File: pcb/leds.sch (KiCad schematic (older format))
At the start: 163 parts, among them K000 1.5U, K001 1U, K002 1U, K003 1U, K004 1U, K005 1U, K006 1U, K007 1U, K008 1U, K009 1U, K010 1U, K011 1U, K012 1U, K013 1.5U, K100 1.5U, K101 1U, K102 1U, K103 1U, K104 1U, K105 1U, K106 1U, K107 1U, K108 1U, K109 1U, K110 1U, K111 1U, K112 1U, K113 1.5U, K200 1.5U, K201 1U, K202 1U, K203 1U, K204 1U, K205 1U, K206 1U, K207 1U, K208 1U, K209 1U, K210 1U, K211 1U, K212 1U, K213 1.5U, K300 1.5U, K301 1U, K302 1U, K303 1U, K304 1U, K305 1U, K306 1U, K307 1U, K308 1U, K309 1U, K310 1U, K311 1U, K312 1U, K313 1.5U, K400 1.5U, K401 1U, K402 1U, K403 1U, K404 1U, K405 1U, K406 1U, K407 1U, K408 1U, K409 1U, K410 1U, K411 1U, K412 1U, K413 1.5U

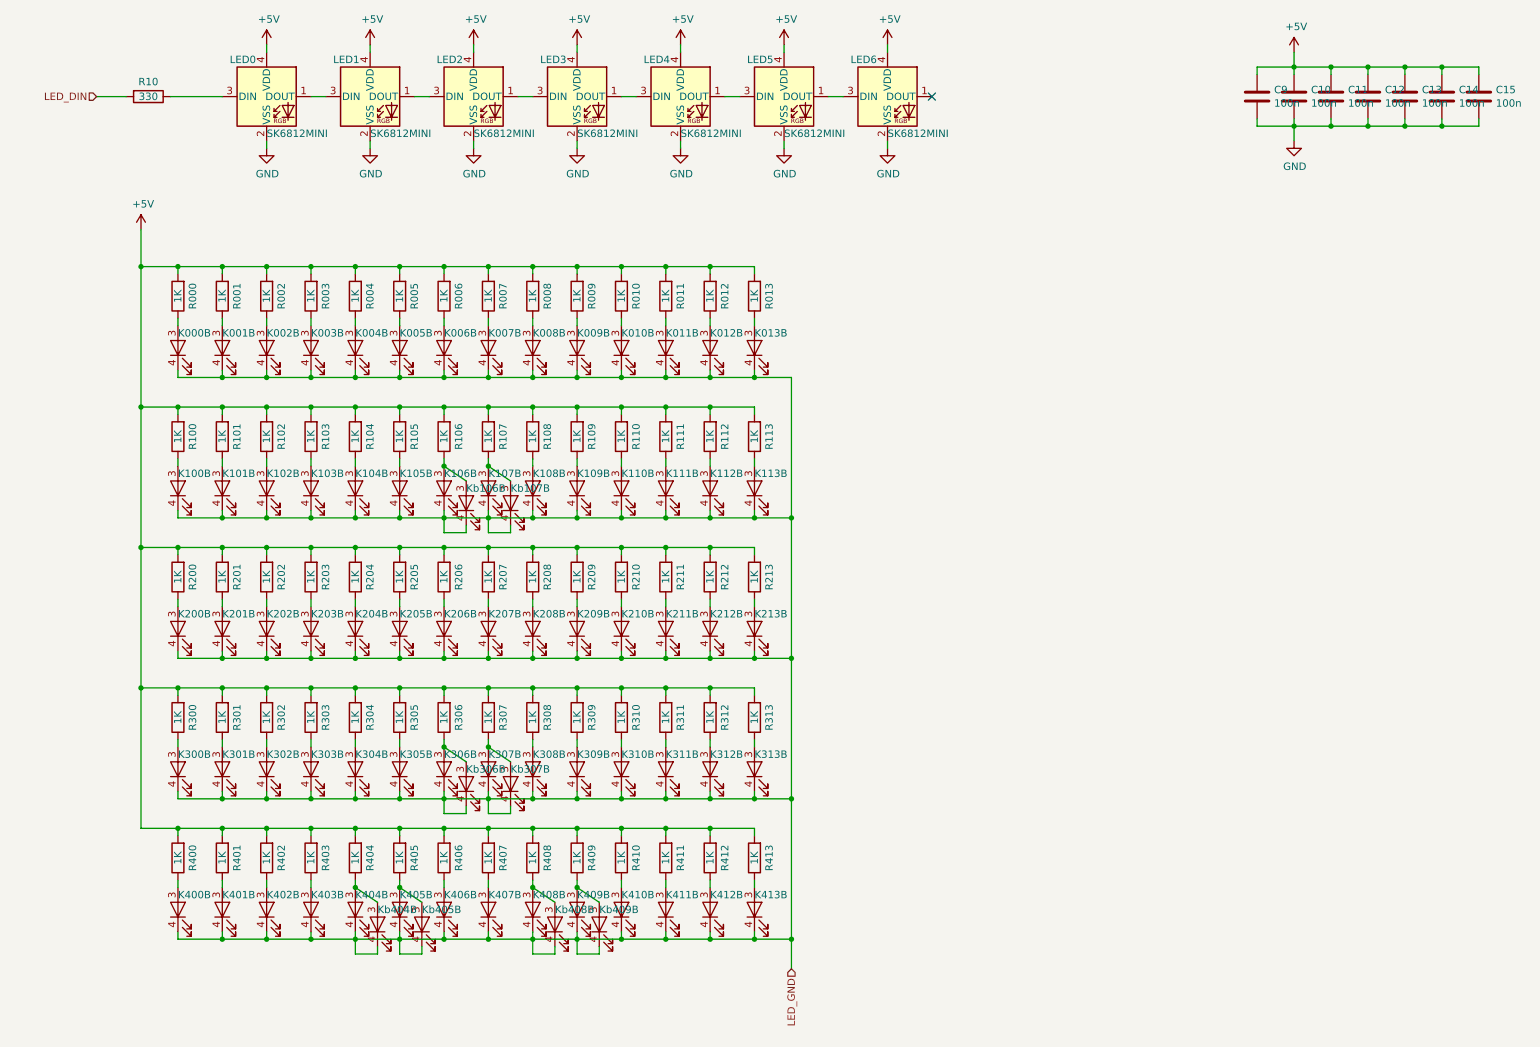
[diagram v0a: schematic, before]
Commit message: IS31 Led matrix
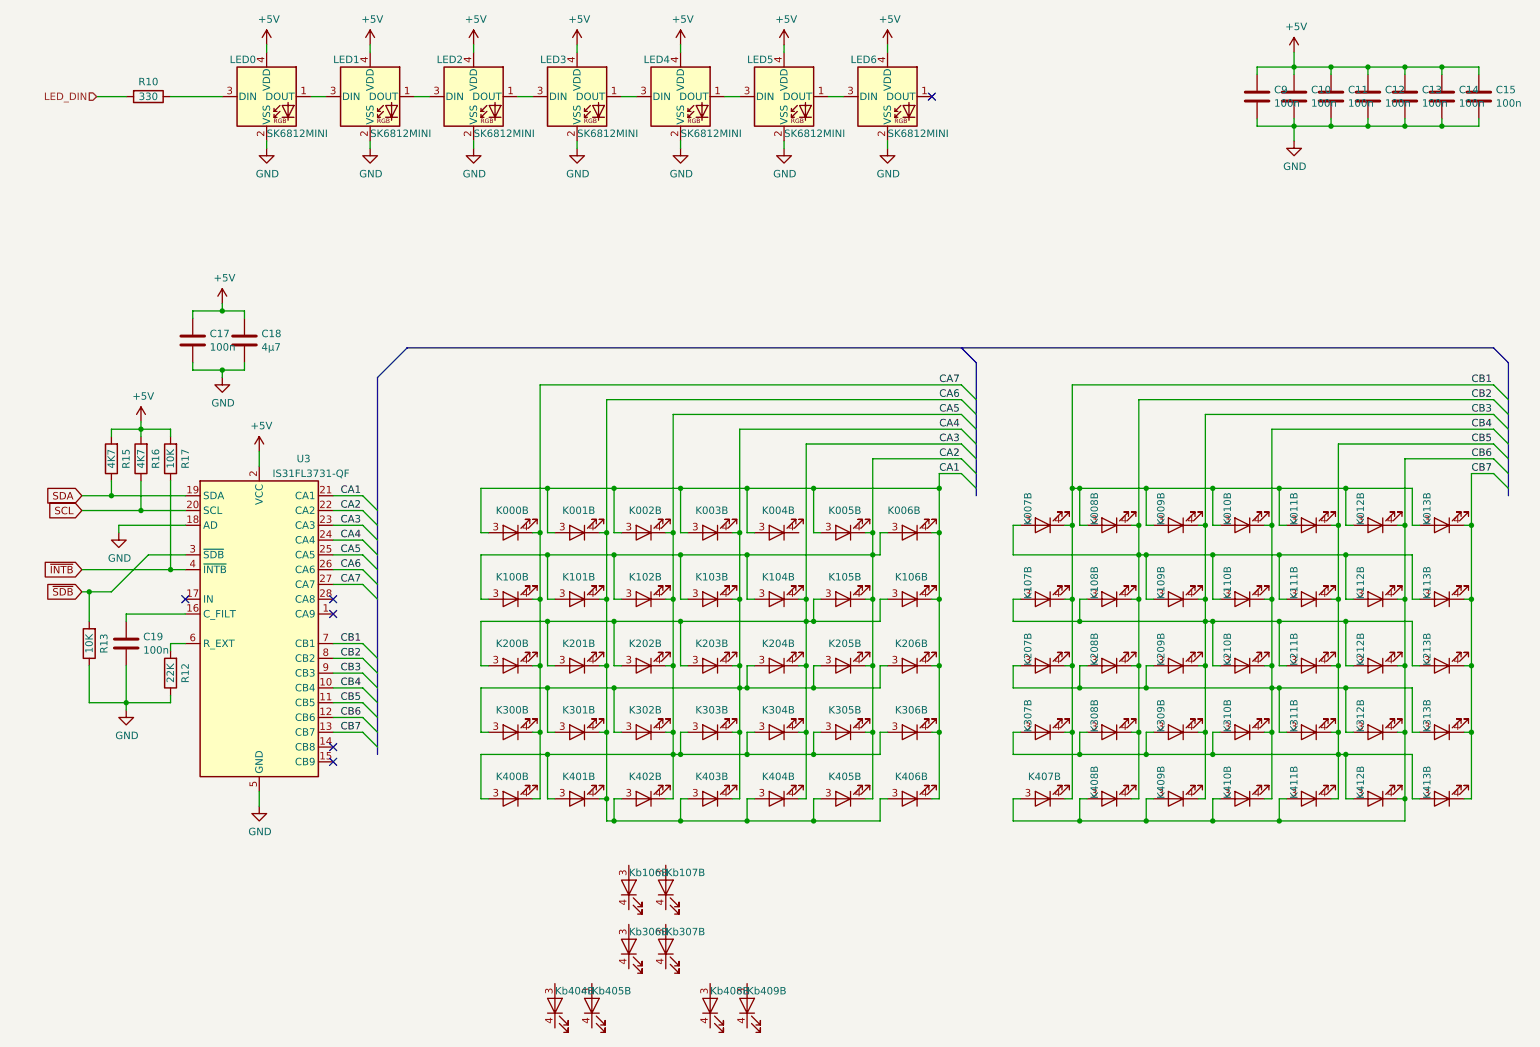
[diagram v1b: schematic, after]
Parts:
- removed R000, R001, R002, R003, R004, R005, R006, R007, R008, R009, R010, R011, R012, R013, R100, R101, R102, R103, R104, R105, R106, R107, R108, R109, R110, R111, R112, R113, R200, R201, R202, R203, R204, R205, R206, R207, R208, R209, R210, R211, R212, R213, R300, R301, R302, R303, R304, R305, R306, R307, R308, R309, R310, R311, R312, R313, R400, R401, R402, R403, R404, R405, R406, R407, R408, R409, R410, R411, R412, R413: 1K, 0xLib_Passive_SMD:R_0603_1608Metric, symbol Device:R
- added C17, C19: 100n, 0xLib_Passive_SMD:C_0603_1608Metric, symbol Device:C
- added C18: 4µ7, 0xLib_Passive_SMD:C_0603_1608Metric, symbol Device:C
- added R12: 22K, 0xLib_Passive_SMD:R_0603_1608Metric, symbol Device:R
- added R13, R17: 10K, 0xLib_Passive_SMD:R_0603_1608Metric, symbol Device:R
- added R15, R16: 4K7, 0xLib_Passive_SMD:R_0603_1608Metric, symbol Device:R
- added U3: IS31FL3731-QF, Package_DFN_QFN:QFN-28-1EP_4x4mm_P0.4mm_EP2.3x2.3mm, symbol Driver_LED:IS31FL3731-QF
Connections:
- net +5V: now also C17.1, C18.1, R15.2, R16.2, R17.2, U3.2 (VCC)
- net GND: now also C17.2, C18.2, C19.2, R12.1, R13.1, U3.18 (AD), U3.29 (GND), U3.5 (GND)
- net CA2: now reaches K100.3 (A)
- net CA2: now also K005.4 (K), K006.3 (A), K101.3 (A), K102.3 (A), K103.3 (A), K104.3 (A), K105.4 (K), K205.4 (K), K305.4 (K), K405.4 (K), U3.22 (CA2)
- net CA3: now reaches K105.3 (A)
- net CA3: now also K104.4 (K), K106.3 (A), K200.3 (A), K201.3 (A), K202.3 (A), K203.3 (A), K204.4 (K), K304.4 (K), K404.4 (K), U3.23 (CA3)
- net at Kb106.3 (A): no longer K106.3 (A)
- net at Kb107.3 (A): no longer K107.3 (A)
- net CB3: now reaches K108.3 (A)
- net CB3: now also K009.4 (K), K107.3 (A), K109.4 (K), K209.4 (K), K210.3 (A), K211.3 (A), K212.3 (A), K213.3 (A), K309.4 (K), K409.4 (K), U3.9 (CB3)
- net CB2: now reaches K109.3 (A)
- net CB2: now also K007.3 (A), K008.4 (K), K108.4 (K), K110.3 (A), K111.3 (A), K112.3 (A), K113.3 (A), K208.4 (K), K308.4 (K), K408.4 (K), U3.8 (CB2)
- net CA4: now reaches K204.3 (A)
- net CA4: now also K003.4 (K), K103.4 (K), K203.4 (K), K205.3 (A), K206.3 (A), K300.3 (A), K301.3 (A), K302.3 (A), K303.4 (K), K403.4 (K), U3.24 (CA4)
- net CB4: now reaches K207.3 (A)
- net CB4: now also K010.4 (K), K110.4 (K), K208.3 (A), K209.3 (A), K210.4 (K), K310.4 (K), K311.3 (A), K312.3 (A), K313.3 (A), K410.4 (K), U3.10 (CB4)
- net CA5: now reaches K303.3 (A)
- net CA5: now also K002.4 (K), K102.4 (K), K202.4 (K), K302.4 (K), K304.3 (A), K305.3 (A), K306.3 (A), K400.3 (A), K401.3 (A), K402.4 (K), U3.25 (CA5)
- net at Kb306.3 (A): no longer K306.3 (A)
- net at Kb307.3 (A): no longer K307.3 (A)
- net CB5: now reaches K308.3 (A)
- net CB5: now also K011.4 (K), K111.4 (K), K211.4 (K), K307.3 (A), K309.3 (A), K310.3 (A), K311.4 (K), K411.4 (K), K412.3 (A), K413.3 (A), U3.11 (CB5)
- net CA1: now reaches K000.3 (A)
- net CA1: now also K001.3 (A), K002.3 (A), K003.3 (A), K004.3 (A), K005.3 (A), K006.4 (K), K106.4 (K), K206.4 (K), K306.4 (K), K406.4 (K), U3.21 (CA1)
- net CA6: now reaches K402.3 (A)
- net CA6: now also K001.4 (K), K101.4 (K), K201.4 (K), K301.4 (K), K401.4 (K), K403.3 (A), K404.3 (A), K405.3 (A), K406.3 (A), U3.26 (CA6)
- net at Kb404.3 (A): no longer K404.3 (A)
- net at Kb405.3 (A): no longer K405.3 (A)
- net CB6: now reaches K407.3 (A)
- net CB6: now also K012.4 (K), K112.4 (K), K212.4 (K), K312.4 (K), K408.3 (A), K409.3 (A), K410.3 (A), K411.3 (A), K412.4 (K), U3.12 (CB6)
- net at Kb408.3 (A): no longer K408.3 (A)
- net at Kb409.3 (A): no longer K409.3 (A)
- net CB1: now reaches K008.3 (A)
- net CB1: now also K007.4 (K), K009.3 (A), K010.3 (A), K011.3 (A), K012.3 (A), K013.3 (A), K107.4 (K), K207.4 (K), K307.4 (K), K407.4 (K), U3.7 (CB1)
- removed net LED_GND: K000.4 (K), K001.4 (K), K002.4 (K), K003.4 (K), K004.4 (K), K005.4 (K), K006.4 (K), K007.4 (K), K008.4 (K), K009.4 (K), K010.4 (K), K011.4 (K), K012.4 (K), K013.4 (K), K100.4 (K), K101.4 (K), K102.4 (K), K103.4 (K), K104.4 (K), K105.4 (K), K106.4 (K), K107.4 (K), K108.4 (K), K109.4 (K), K110.4 (K), K111.4 (K), K112.4 (K), K113.4 (K), K200.4 (K), K201.4 (K), K202.4 (K), K203.4 (K), K204.4 (K), K205.4 (K), K206.4 (K), K207.4 (K), K208.4 (K), K209.4 (K), K210.4 (K), K211.4 (K), K212.4 (K), K213.4 (K), K300.4 (K), K301.4 (K), K302.4 (K), K303.4 (K), K304.4 (K), K305.4 (K), K306.4 (K), K307.4 (K), K308.4 (K), K309.4 (K), K310.4 (K), K311.4 (K), K312.4 (K), K313.4 (K), K400.4 (K), K401.4 (K), K402.4 (K), K403.4 (K), K404.4 (K), K405.4 (K), K406.4 (K), K407.4 (K), K408.4 (K), K409.4 (K), K410.4 (K), K411.4 (K), K412.4 (K), K413.4 (K), Kb106.4 (K), Kb107.4 (K), Kb306.4 (K), Kb307.4 (K), Kb404.4 (K), Kb405.4 (K), Kb408.4 (K), Kb409.4 (K)
- new net: C19.1, U3.16 (C_FILT)
- new net: R12.2, U3.6 (R_EXT)
- new net CA7: K000.4 (K), K100.4 (K), K200.4 (K), K300.4 (K), K400.4 (K), U3.27 (CA7)
- new net CB7: K013.4 (K), K113.4 (K), K213.4 (K), K313.4 (K), K413.4 (K), U3.13 (CB7)
- new net SCL: R16.1, U3.20 (SCL)
- new net SDA: R15.1, U3.19 (SDA)
- new net ~INTB: R17.1, U3.4 (~INTB)
- new net ~SDB: R13.2, U3.3 (~SDB)
- no-connect marks 1 -> 6
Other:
- moved on the sheet: K000B, K001B, K002B, K003B, K004B, K005B, K006B, K007B, K008B, K009B, K010B, K011B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

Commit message: Complete STM32 PCB v1
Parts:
- removed C17, C19: 100n, 0xLib_Passive_SMD:C_0603_1608Metric, symbol Device:C
- removed C18: 4µ7, 0xLib_Passive_SMD:C_0603_1608Metric, symbol Device:C
- removed K000, Kb106, Kb107, Kb306, Kb307: 1.5U, 0xLib_MK_Switches:MXOnly-1.5U-Vertical, symbol 0xLib_MK:Key_Switch_LED
- removed K001, K002, K003, K004, K005, K006, K007, K008, K009, K010, K011, K012, K101, K102, K103, K104, K105, K106, K107, K108, K109, K110, K111, K112, K201, K202, K203, K204, K205, K206, K207, K208, K209, K210, K211, K212, K301, K302, K303, K304, K305, K306, K307, K308, K309, K310, K311, K312, K401, K402, K403, K404, K405, K406, K407, K408, K409, K410, K411, K412: 1U, 0xLib_MK_Switches:MXOnly-1U, symbol 0xLib_MK:Key_Switch_LED
- removed K013, K100, K113, K200, K213, K300, K313, K400, K413: 1.5U, 0xLib_MK_Switches:MXOnly-1.5U, symbol 0xLib_MK:Key_Switch_LED
- removed Kb404, Kb405, Kb408, Kb409: 2U, 0xLib_MK_Switches:MXOnly-2U-ReversedStabilizers, symbol 0xLib_MK:Key_Switch_LED
- removed R12: 22K, 0xLib_Passive_SMD:R_0603_1608Metric, symbol Device:R
- removed R13, R17: 10K, 0xLib_Passive_SMD:R_0603_1608Metric, symbol Device:R
- removed R15, R16: 4K7, 0xLib_Passive_SMD:R_0603_1608Metric, symbol Device:R
- removed U3: IS31FL3731-QF, Package_DFN_QFN:QFN-28-1EP_4x4mm_P0.4mm_EP2.3x2.3mm, symbol Driver_LED:IS31FL3731-QF
- renumbered C11 to C17, C12 to C18, C13 to C19, C14 to C20, C15 to C21, C9 to C22, C10 to C23, R10 to R9
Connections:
- no-connect marks 6 -> 1
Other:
- moved on the sheet: C17, C18, C19, C20, C21, C22, C23, LED0, LED1, LED2, LED3, LED4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
